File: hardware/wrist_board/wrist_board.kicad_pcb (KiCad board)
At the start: 4 copper layers, 60 x 40 mm, 45 parts, among them J1 S2B-PH-K-S_LF__SN_, J2 USB_C_Receptacle_USB2.0_14P, J3 Conn_01x02, J4 Conn_01x02, J5 Conn_01x02, J6 Conn_01x02, J7 Conn_01x02, SW1 SW_SPST, U1 MCP73831T-2ACI_OT, U2 TLV75533PDBV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

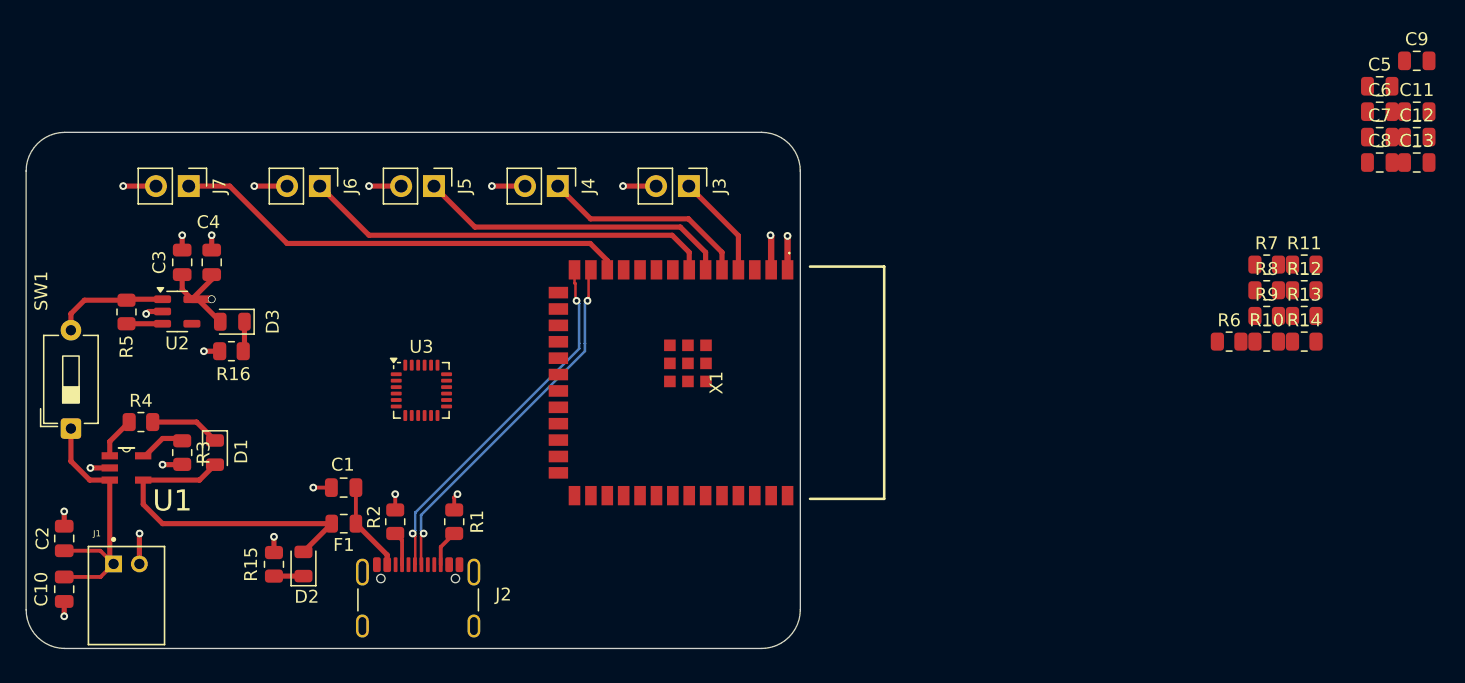
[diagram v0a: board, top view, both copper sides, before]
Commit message: Added SDA and SCL routing/pullups
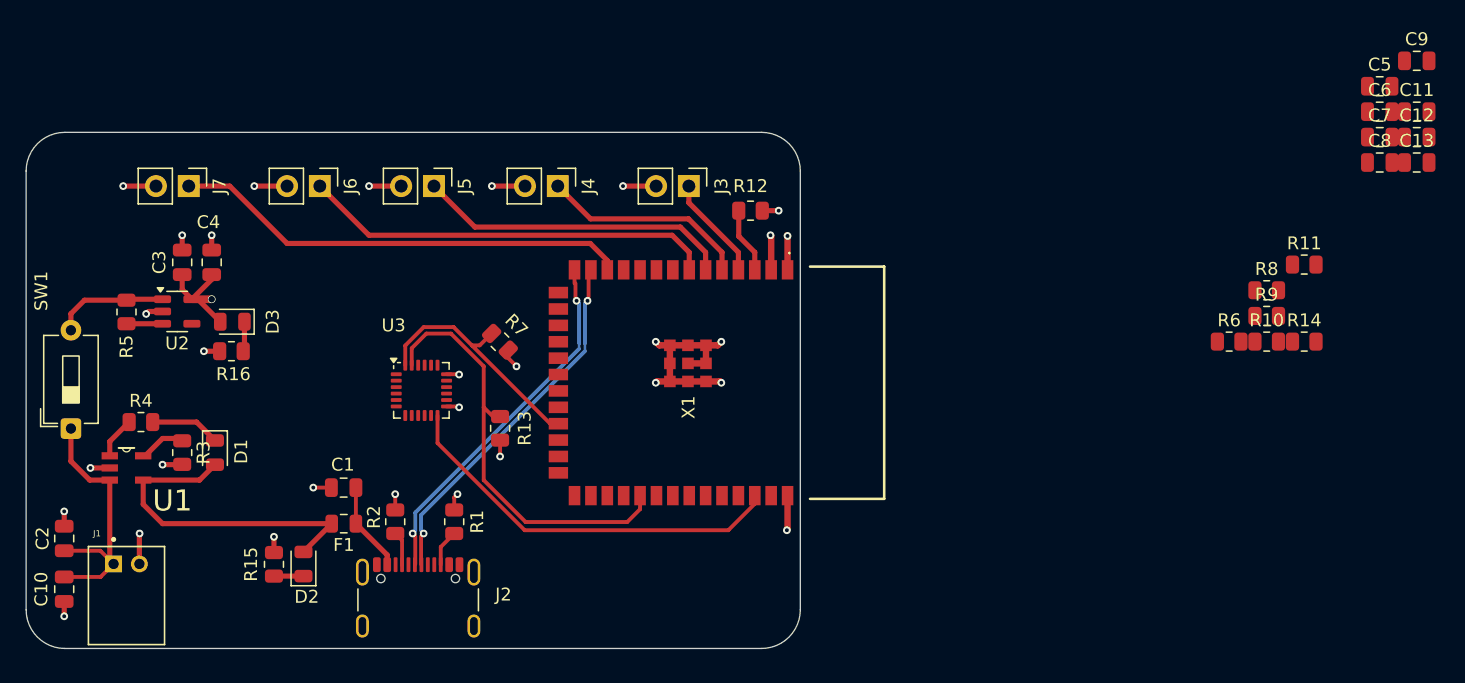
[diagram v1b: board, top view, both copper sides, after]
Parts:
- moved R13 62.9 mm to (102.9, 110.2), turned to 90 degrees
- moved R7 59.7 mm to (102.9, 103.5), turned to 135 degrees
- moved R12 43.4 mm to (122.3, 93.3), turned to 180 degrees
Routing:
- net /SCL: track 0.00 -> 33.7 mm
- net /INT: track 0.00 -> 31.0 mm
- net GND: track 33.1 -> 52.9 mm, vias 19 -> 25
- net /SDA: track 0.00 -> 19.0 mm
- net Net-(X1-EN): track 0.00 -> 5.10 mm
- net +3V3: track 11.9 -> 17.0 mm, vias 2 -> 6

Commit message: Added voltage divider resistors for flex sensors
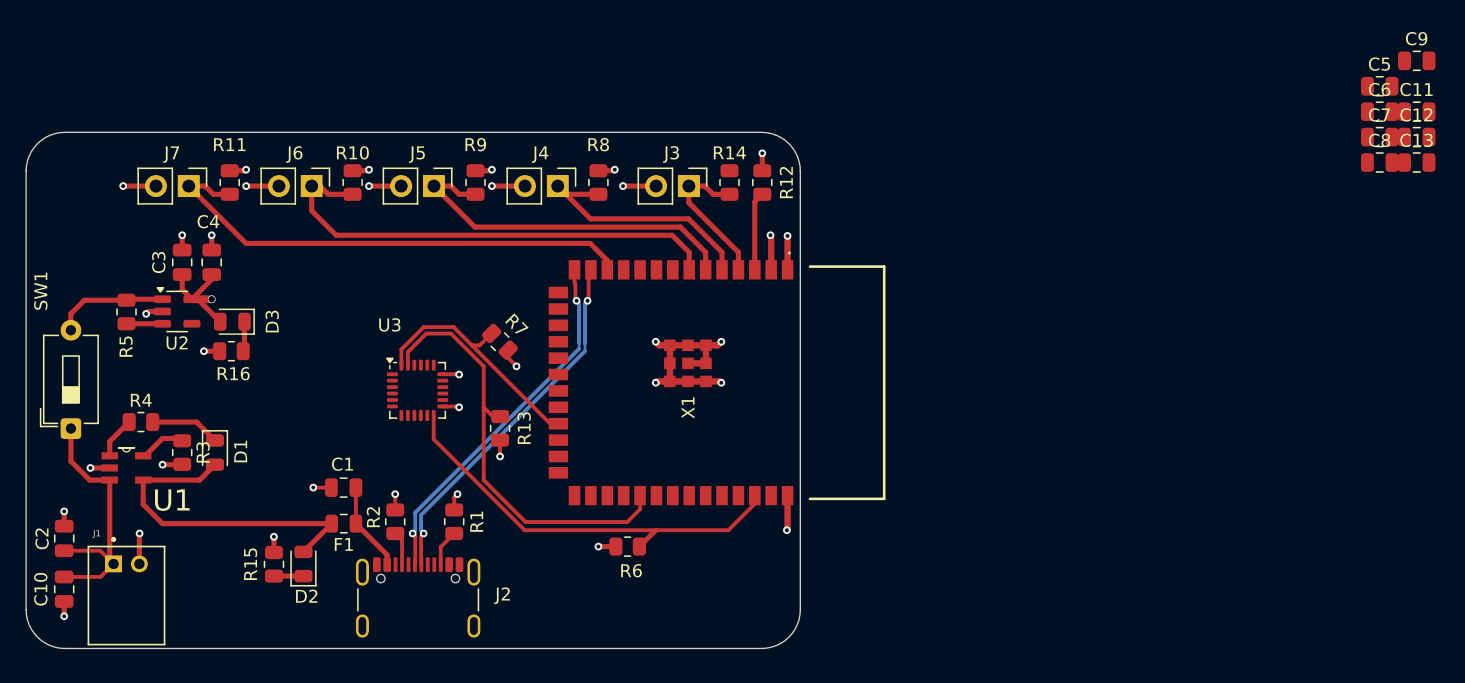
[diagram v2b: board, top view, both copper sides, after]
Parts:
- moved R11 83.5 mm to (81.9, 91.2), turned to 90 degrees
- moved R10 71.9 mm to (91.4, 91.2), turned to 90 degrees
- moved R9 62.2 mm to (101.0, 91.2), turned to 90 degrees
- moved R8 52.5 mm to (110.5, 91.2), turned to 90 degrees
- moved R6 49.3 mm to (112.8, 119.4)
- moved R14 46.2 mm to (120.7, 91.2), turned to 90 degrees
- moved R12 2.37 mm to (123.2, 91.2), turned to -90 degrees
- moved J6 0.63 mm to (88.3, 91.4)
- moved U3 0.30 mm to (96.5, 107.3)
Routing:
- net +3V3: track 17.0 -> 23.9 mm, vias 6 -> 11
- net /FS_4: track 32.1 -> 37.3 mm
- net /FS_3: track 24.5 -> 28.0 mm
- net /FS_5: track 35.5 -> 39.0 mm
- net /FS_1: track 8.08 -> 11.5 mm
- net /FS_2: track 16.2 -> 19.6 mm
- net /INT: track 31.0 -> 32.9 mm
- net Net-(X1-EN): track 5.10 -> 6.10 mm

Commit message: All major components routed, still needs extra GPIO pinouts
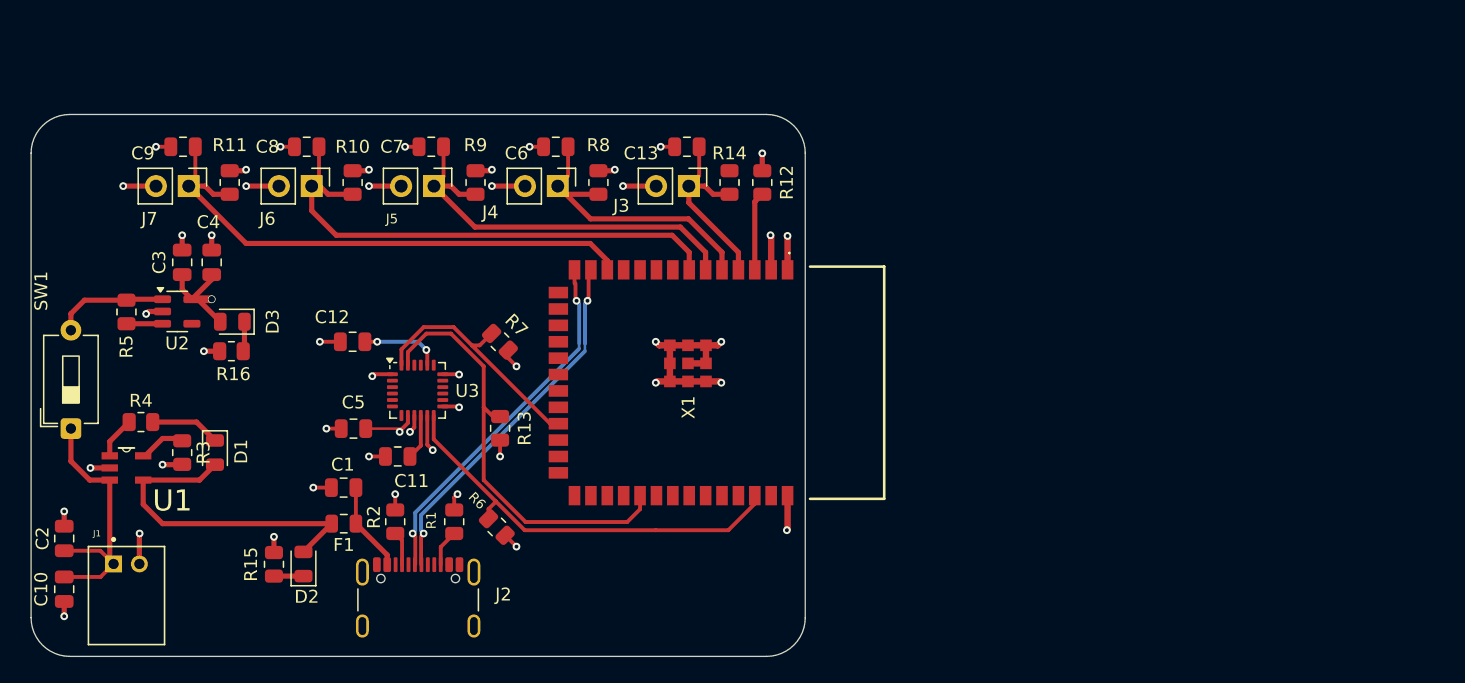
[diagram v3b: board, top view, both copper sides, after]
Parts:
- moved C9 95.8 mm to (78.3, 88.4), turned to 180 degrees
- moved C12 84.0 mm to (91.4, 103.5), turned to 180 degrees
- moved C5 83.8 mm to (91.5, 110.2), turned to 180 degrees
- moved C11 83.4 mm to (94.9, 112.4), turned to 180 degrees
- moved C8 83.2 mm to (87.9, 88.4), turned to 180 degrees
- moved C7 73.5 mm to (97.5, 88.4), turned to 180 degrees
- moved C6 63.9 mm to (107.2, 88.4), turned to 180 degrees
- moved C13 56.6 mm to (117.3, 88.4), turned to 180 degrees
- moved R6 10.3 mm to (102.6, 117.9), turned to 135 degrees
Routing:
- net GND: track 53.2 -> 68.6 mm, vias 25 -> 36
- net Net-(U3-CPOUT): track 0.00 -> 6.24 mm, vias 0 -> 2
- net +3V3: track 23.9 -> 28.8 mm, vias 11 -> 12
- net Net-(U3-REGOUT): track 0.00 -> 3.52 mm
- net /FS_1: track 11.5 -> 14.9 mm
- net /FS_2: track 19.6 -> 23.0 mm
- net /FS_3: track 28.0 -> 31.4 mm
- net /FS_4: track 37.3 -> 40.6 mm
- net /FS_5: track 39.0 -> 42.2 mm
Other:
- board size 60 x 40 mm -> 60 x 42 mm

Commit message: Added boot and reset buttons in schematic
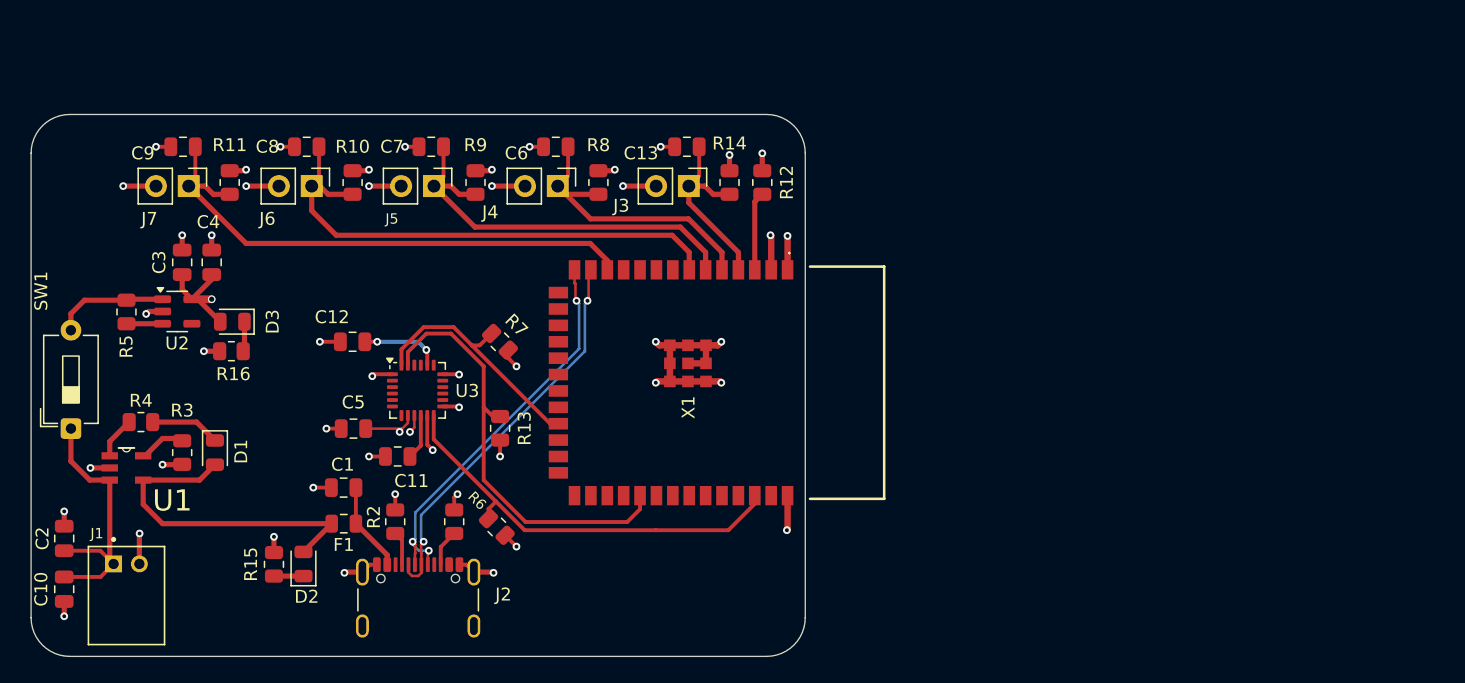
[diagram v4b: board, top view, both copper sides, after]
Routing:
- net GND: track 68.6 -> 74.2 mm, vias 36 -> 38
- net /D+: track 28.5 -> 31.3 mm, vias 2 -> 3
- net /D-: track 28.5 -> 31.0 mm
- net +3V3: track 28.8 -> 29.4 mm, vias 12 -> 13

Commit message: Added test points to layout
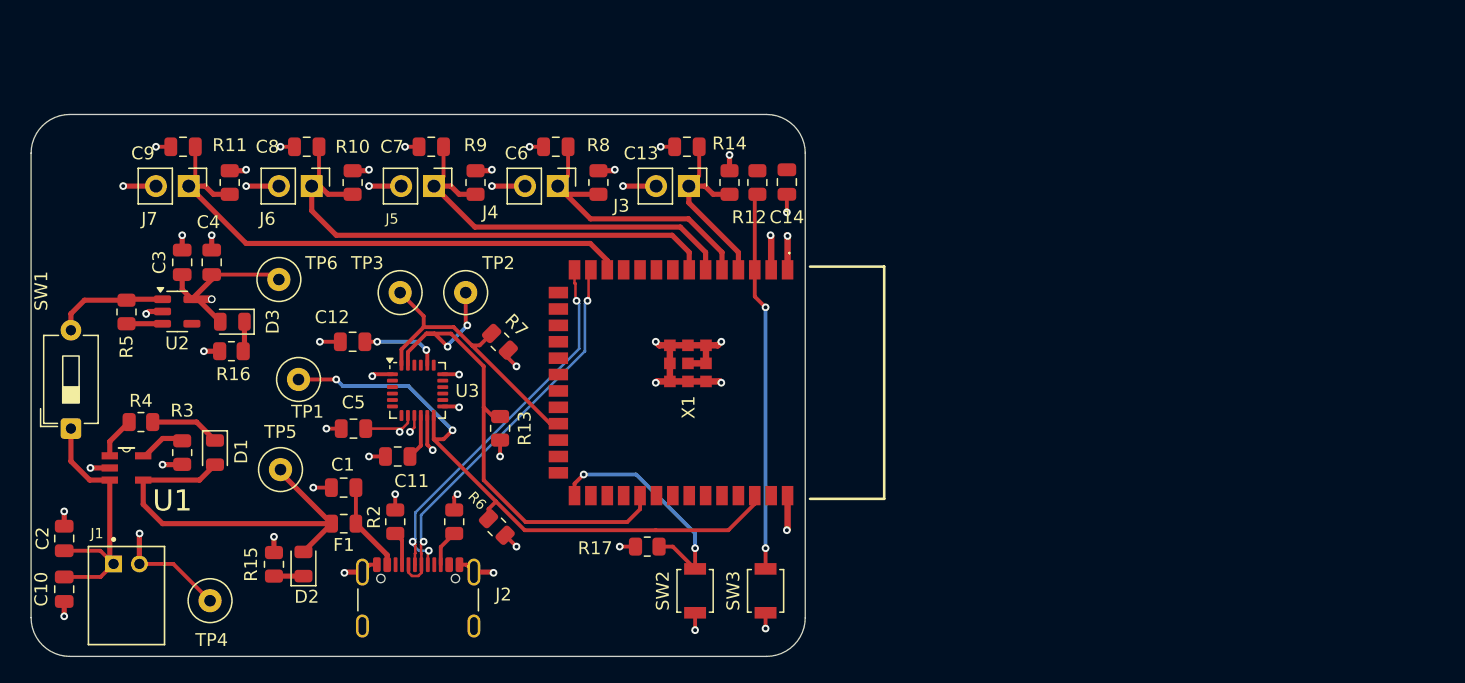
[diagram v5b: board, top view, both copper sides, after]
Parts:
- added C14: 0.1uF, Capacitor_SMD:C_0805_2012Metric, F.Cu at (125.1, 91.1)
- added R17: 10k, Resistor_SMD:R_0805_2012Metric, F.Cu at (114.3, 119.4)
- added SW2: BOOT_BTN, Button_Switch_SMD:SW_SPST_B3U-1000P, F.Cu at (118.0, 122.8)
- added SW3: RST_BTN, Button_Switch_SMD:SW_SPST_B3U-1000P, F.Cu at (123.4, 122.8)
- added TP1: INT_TP, TestPoint:TestPoint_Loop_D2.60mm_Drill0.9mm_Beaded, F.Cu at (87.2, 106.4)
- added TP2: SCL_TP, TestPoint:TestPoint_Loop_D2.60mm_Drill0.9mm_Beaded, F.Cu at (100.2, 99.7)
- added TP3: SDA_TP, TestPoint:TestPoint_Loop_D2.60mm_Drill0.9mm_Beaded, F.Cu at (95.1, 99.7)
- added TP4: GND_TP, TestPoint:TestPoint_Loop_D2.60mm_Drill0.9mm_Beaded, F.Cu at (80.4, 123.6)
- added TP5: 5V_TP, TestPoint:TestPoint_Loop_D2.60mm_Drill0.9mm_Beaded, F.Cu at (85.9, 113.4)
- added TP6: 3V3_TP, TestPoint:TestPoint_Loop_D2.60mm_Drill0.9mm_Beaded, F.Cu at (85.7, 98.7)
- moved R12 0.38 mm to (122.8, 91.2), turned to 90 degrees
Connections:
- R12 pad 1: +3V3 -> /EN
- R12 pad 2: Net-(X1-EN) -> +3V3
- X1 pad 10: unconnected-(X1-IO17-Pad10) -> /IO17
- X1 pad 11: unconnected-(X1-IO18-Pad11) -> /IO18
- X1 pad 17: unconnected-(X1-IO9-Pad17) -> /IO9
- X1 pad 18: unconnected-(X1-IO10-Pad18) -> /IO10
- X1 pad 19: unconnected-(X1-IO11-Pad19) -> /IO11
- X1 pad 20: unconnected-(X1-IO12-Pad20) -> /IO12
- X1 pad 21: unconnected-(X1-IO13-Pad21) -> /IO13
- X1 pad 22: unconnected-(X1-IO14-Pad22) -> /IO14
- X1 pad 27: unconnected-(X1-IO0-Pad27) -> /BOOT
- X1 pad 3: Net-(X1-EN) -> /EN
- X1 pad 8: unconnected-(X1-IO15-Pad8) -> /IO15
- X1 pad 9: unconnected-(X1-IO16-Pad9) -> /IO16
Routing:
- net /EN: track 0.00 -> 29.5 mm, vias 0 -> 2
- net /BOOT: track 0.00 -> 18.7 mm, vias 0 -> 2
- net /INT: track 32.7 -> 48.0 mm, vias 0 -> 2
- net GND: track 74.2 -> 84.9 mm, vias 38 -> 41
- net /SCL: track 33.8 -> 40.8 mm, vias 0 -> 2
- net Net-(X1-EN): track 6.10 -> 0.00 mm
- net +5V: track 26.3 -> 32.1 mm
- net +3V3: track 29.4 -> 34.6 mm
- net /SDA: track 19.1 -> 22.5 mm

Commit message: Test points and extra GPIOs added to layout
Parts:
- added J8: GPIOs, Connector_PinHeader_2.54mm:PinHeader_2x02_P2.54mm_Vertical, F.Cu at (110.0, 121.4)
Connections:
- X1 pad 10: /IO17 -> unconnected-(X1-IO17-Pad10)
- X1 pad 11: /IO18 -> unconnected-(X1-IO18-Pad11)
- X1 pad 17: /IO9 -> unconnected-(X1-IO9-Pad17)
- X1 pad 18: /IO10 -> unconnected-(X1-IO10-Pad18)
- X1 pad 8: /IO15 -> unconnected-(X1-IO15-Pad8)
- X1 pad 9: /IO16 -> unconnected-(X1-IO16-Pad9)
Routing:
- net /IO13: track 0.00 -> 21.5 mm, vias 0 -> 1
- net /IO12: track 0.00 -> 20.8 mm, vias 0 -> 1
- net /IO11: track 0.00 -> 19.5 mm, vias 0 -> 1
- net /IO14: track 0.00 -> 14.3 mm, vias 0 -> 1

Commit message: Minor changes to pass DRC
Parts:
- renumbered SW2 to BOOT, SW3 to RESET
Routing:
- net Net-(C1-Pad1): track 6.98 -> 13.4 mm
- net +3V3: track 34.6 -> 37.0 mm, vias 13 -> 15
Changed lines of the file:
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@@
 		(descr "Ultra-small-sized Tactile Switch with High Contact Reliability, Top-actuated Model, without Ground Terminal, without Boss")
 		(tags "Tactile Switch")
-		(property "Reference" "SW3"
-			(at 0 -2.5 90)
+		(property "Reference" "RESET"
+			(at 0 -2.54 90)
 			(layer "F.SilkS")
 			(effects
@@
 		(tags "resistor")
 		(property "Reference" "R17"
-			(at 4.0405 -0.127 0)
+			(at 0.9925 -1.778 0)
 			(layer "F.SilkS")
 			(effects
@@
 			(layer "F.Fab")
 		)
-		(fp_text user "${REFERENCE}"
-			(at 0 0 0)
-			(layer "F.Fab")
-			(effects
-				(font
-					(size 0.5 0.5)
-					(thickness 0.08)
-				)
-			)
-		)
 		(pad "1" smd roundrect
 			(at -0.9125 0 180)
@@
 		(tags "USB C Type-C Receptacle SMD USB 2.0 16P 16C USB4105-15-A USB4105-15-A-060 USB4105-15-A-120 USB4105-GF-A USB4105-GF-A-060 USB4105-GF-A-120")
 		(property "Reference" "J2"
-			(at 6.606 -1.3634 0)
+			(at 6.223 2.286 0)
 			(unlocked yes)
 			(layer "F.SilkS")
@@
 		(descr "Ultra-small-sized Tactile Switch with High Contact Reliability, Top-actuated Model, without Ground Terminal, without Boss")
 		(tags "Tactile Switch")
-		(property "Reference" "SW2"
-			(at 0 -2.5 90)
+		(property "Reference" "BOOT"
+			(at 0 -2.54 90)
 			(layer "F.SilkS")
 			(effects
@@
 	)
 	(segment
-		(start 99.72 120.78)
-		(end 100.265 120.78)
+		(start 100.265 120.78)
+		(end 99.72 120.78)
 		(width 0.3)
 		(layer "F.Cu")
@@
 	)
 	(segment
+		(start 122.809 90.25)
+		(end 122.809 89.027)
+		(width 0.3)
+		(layer "F.Cu")
+		(net 3)
+	)
+	(segment
 		(start 99.63 108.52)
 		(end 99.695 108.585)
@@
 	)
 	(segment
+		(start 125.095 90.175)
+		(end 125.095 89.027)
+		(width 0.3)
+		(layer "F.Cu")
+		(net 3)
+	)
+	(segment
 		(start 95.725 109.22)
 		(end 95.725 109.800057)
@@
 	)
 	(via
+		(at 125.095 89.027)
+		(size 0.6)
+		(drill 0.3)
+		(layers "F.Cu" "B.Cu")
+		(net 3)
+	)
+	(via
 		(at 92.71 90.17)
 		(size 0.6)
@@
 		(net 3)
 	)
+	(via
+		(at 122.809 89.027)
+		(size 0.6)
+		(drill 0.3)
+		(layers "F.Cu" "B.Cu")
+		(net 3)
+	)
 	(segment
 		(start 106.75352 109.855)
@@
 	)
 	(segment
+		(start 94.879 122.057)
+		(end 98.101824 122.057)
+		(width 0.2)
+		(layer "F.Cu")
+		(net 38)
+	)
+	(segment
+		(start 98.101824 122.057)
+		(end 98.92 121.238824)
+		(width 0.2)
+		(layer "F.Cu")
+		(net 38)
+	)
+	(segment
 		(start 94.12 120.028)
 		(end 91.694 117.602)
@@
 	)
 	(segment
+		(start 98.92 121.238824)
+		(end 98.92 120.78)
+		(width 0.2)
+		(layer "F.Cu")
+		(net 38)
+	)
+	(segment
 		(start 91.694 114.808)
 		(end 91.694 117.602)
@@
 		(layer "F.Cu")
 		(net 38)
+	)
+	(segment
+		(start 94.12 120.78)
+		(end 94.12 121.298)
+		(width 0.2)
+		(layer "F.Cu")
+		(net 38)
+	)
+	(segment
+		(start 94.12 121.298)
+		(end 94.879 122.057)
+		(width 0.2)
+		(layer "F.Cu")
+		(net 38)
